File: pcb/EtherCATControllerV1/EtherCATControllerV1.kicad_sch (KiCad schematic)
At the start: 0 parts

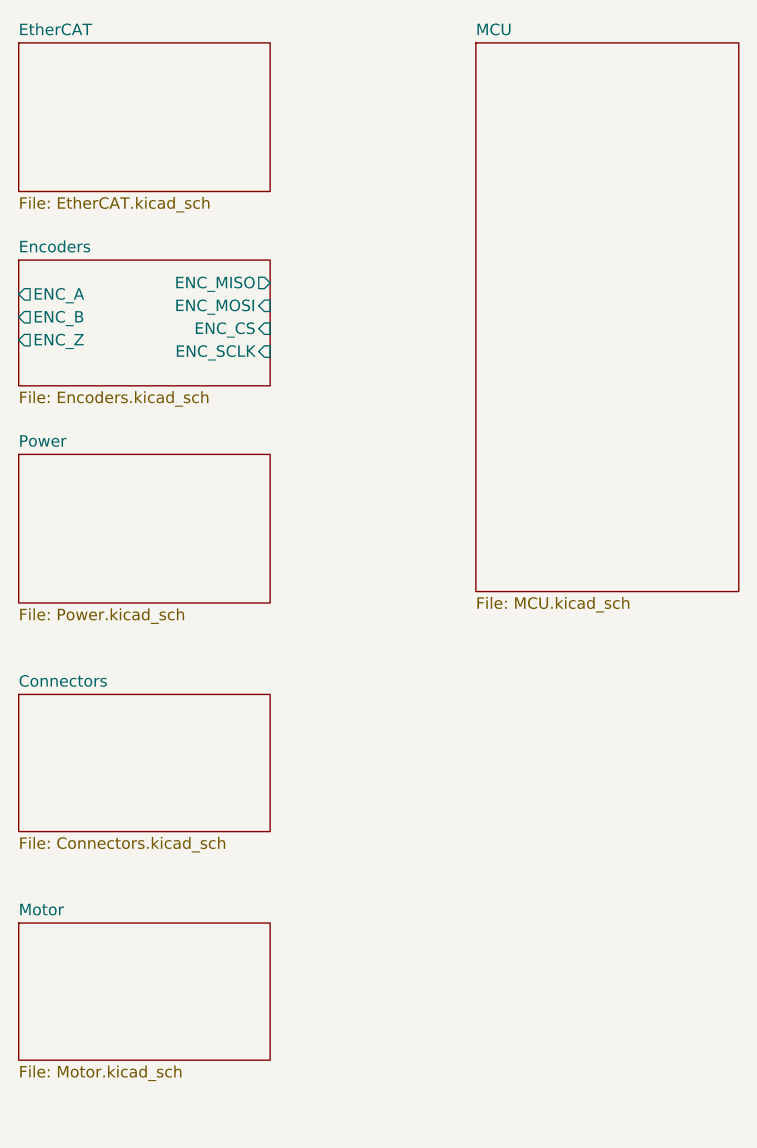
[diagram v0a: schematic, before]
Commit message: Initial design without Ethernet connectors
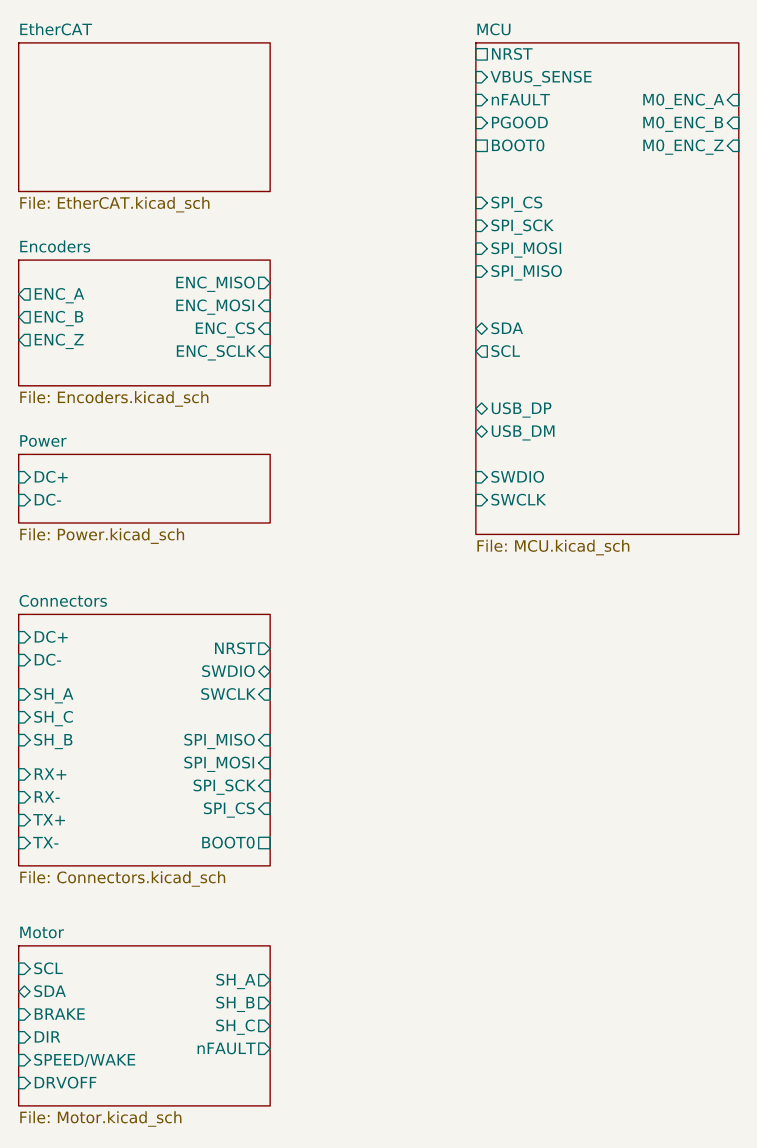
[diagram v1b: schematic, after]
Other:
- sheet Connectors ports: added BOOT0, DC+, DC-, NRST, RX+, RX-, SH_A, SH_B, SH_C, SPI_CS, SPI_MISO, SPI_MOSI, SPI_SCK, SWCLK, SWDIO, TX+, TX-; removed none
- sheet MCU ports: added BOOT0, M0_ENC_A, M0_ENC_B, M0_ENC_Z, NRST, PGOOD, SCL, SDA, SPI_CS, SPI_MISO, SPI_MOSI, SPI_SCK, SWCLK, SWDIO, USB_DM, USB_DP, VBUS_SENSE, nFAULT; removed none
- sheet Motor ports: added BRAKE, DIR, DRVOFF, SCL, SDA, SH_A, SH_B, SH_C, SPEED/WAKE, nFAULT; removed none
- sheet Power ports: added DC+, DC-; removed none

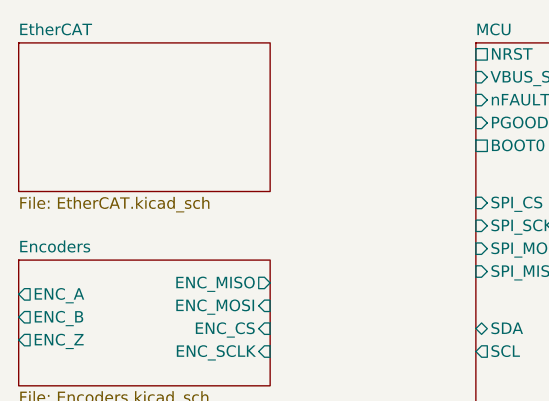
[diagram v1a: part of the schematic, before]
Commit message: Added IO Board project
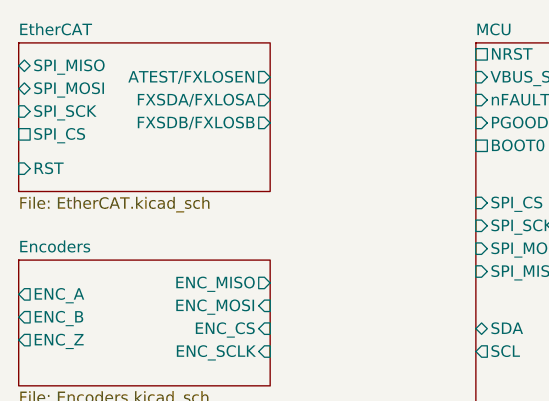
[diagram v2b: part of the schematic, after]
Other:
- sheet EtherCAT ports: added ATEST/FXLOSEN, FXSDA/FXLOSA, FXSDB/FXLOSB, RST, SPI_CS, SPI_MISO, SPI_MOSI, SPI_SCK; removed none
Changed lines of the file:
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@@
+			)
+		)
+		(pin "SPI_MISO" bidirectional
+			(at 38.1 27.94 180)
+			(effects
+				(font
+					(size 1.27 1.27)
+				)
+				(justify left)
+			)
+		)
+		(pin "SPI_MOSI" bidirectional
+			(at 38.1 30.48 180)
+			(effects
+				(font
+					(size 1.27 1.27)
+				)
+				(justify left)
+			)
+		)
+		(pin "SPI_SCK" input
+			(at 38.1 33.02 180)
+			(effects
+				(font
+					(size 1.27 1.27)
+				)
+				(justify left)
+			)
+		)
+		(pin "RST" input
+			(at 38.1 39.37 180)
+			(effects
+				(font
+					(size 1.27 1.27)
+				)
+				(justify left)
+			)
+		)
+		(pin "ATEST{slash}FXLOSEN" output
+			(at 66.04 29.21 0)
+			(effects
+				(font
+					(size 1.27 1.27)
+				)
+				(justify right)
+			)
+		)
+		(pin "FXSDB{slash}FXLOSB" output
+			(at 66.04 34.29 0)
+			(effects
+				(font
+					(size 1.27 1.27)
+				)
+				(justify right)
+			)
+		)
+		(pin "FXSDA{slash}FXLOSA" output
+			(at 66.04 31.75 0)
+			(effects
+				(font
+					(size 1.27 1.27)
+				)
+				(justify right)
+			)
+		)
+		(pin "SPI_CS" passive
+			(at 38.1 35.56 180)
+			(effects
+				(font
+					(size 1.27 1.27)
+				)
+				(justify left)
 			)
 		)

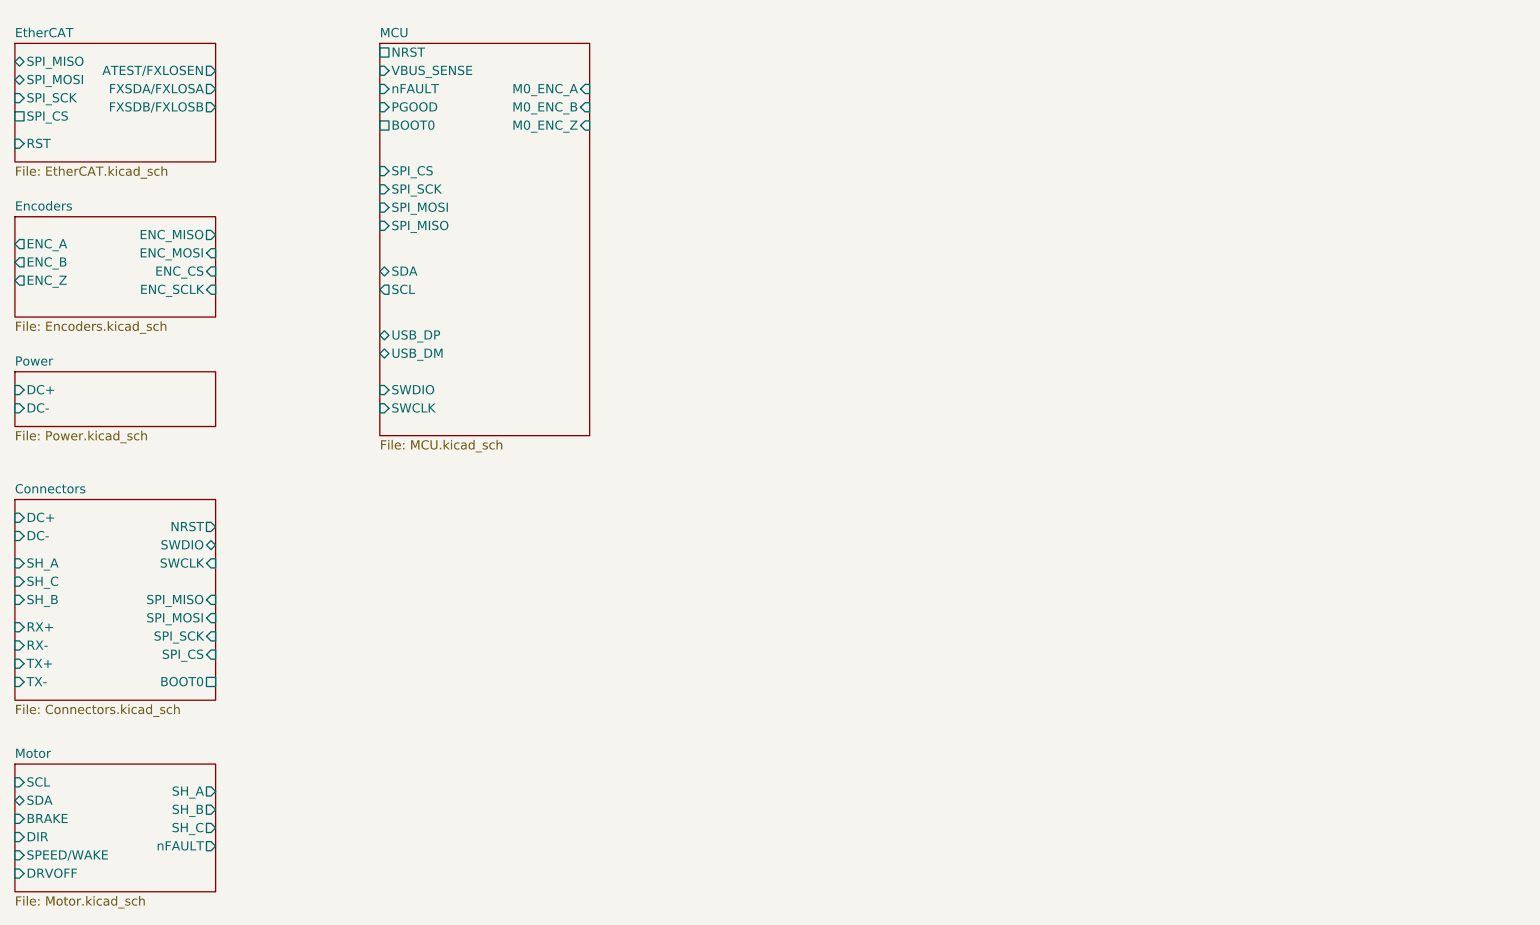
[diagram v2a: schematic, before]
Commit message: schematic finished, need to set proper ERCs
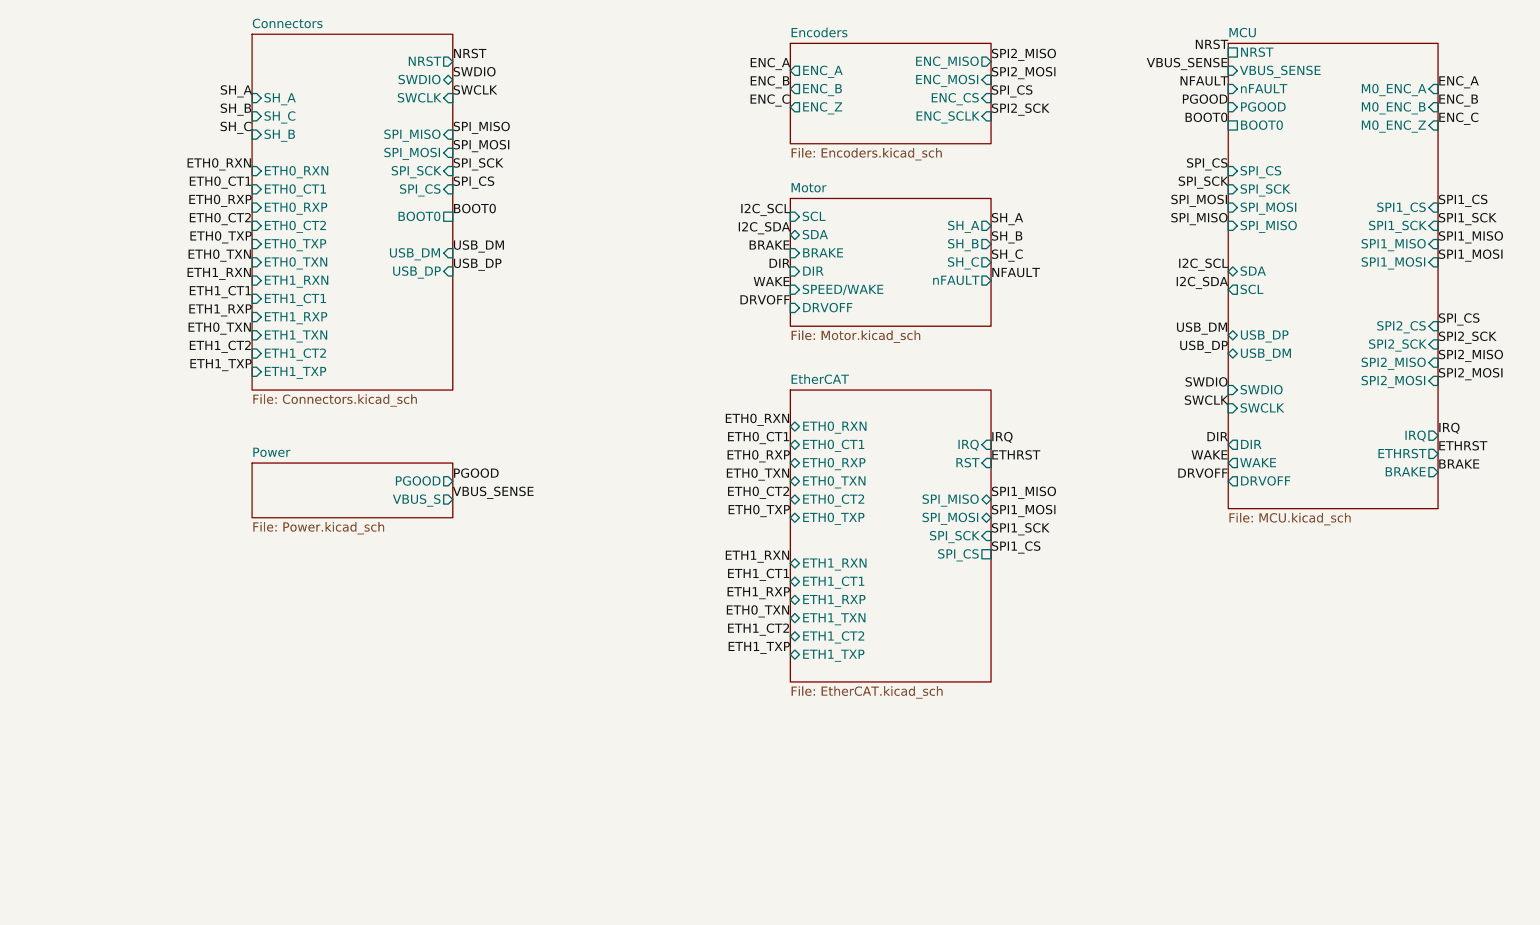
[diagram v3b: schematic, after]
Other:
- sheet Connectors ports: added ETH0_CT1, ETH0_CT2, ETH0_RXN, ETH0_RXP, ETH0_TXN, ETH0_TXP, ETH1_CT1, ETH1_CT2, ETH1_RXN, ETH1_RXP, ETH1_TXN, ETH1_TXP, USB_DM, USB_DP; removed DC+, DC-, RX+, RX-, TX+, TX-
- sheet EtherCAT ports: added ETH0_CT1, ETH0_CT2, ETH0_RXN, ETH0_RXP, ETH0_TXN, ETH0_TXP, ETH1_CT1, ETH1_CT2, ETH1_RXN, ETH1_RXP, ETH1_TXN, ETH1_TXP, IRQ; removed ATEST/FXLOSEN, FXSDA/FXLOSA, FXSDB/FXLOSB
- sheet MCU ports: added BRAKE, DIR, DRVOFF, ETHRST, IRQ, SPI1_CS, SPI1_MISO, SPI1_MOSI, SPI1_SCK, SPI2_CS, SPI2_MISO, SPI2_MOSI, SPI2_SCK, WAKE; removed none
- sheet Power ports: added PGOOD, VBUS_S; removed DC+, DC-

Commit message: Added more BOM items
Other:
- sheet MCU ports: added NFAULT; removed nFAULT
- sheet Motor ports: added NFAULT; removed nFAULT
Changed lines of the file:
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@@
-			)
-		)
-		(pin "nFAULT" output
-			(at 173.99 58.42 0)
-			(effects
-				(font
-					(size 1.27 1.27)
-				)
-				(justify right)
 			)
 		)
@@
 				)
 				(justify left)
+			)
+		)
+		(pin "NFAULT" output
+			(at 173.99 58.42 0)
+			(effects
+				(font
+					(size 1.27 1.27)
+				)
+				(justify right)
 			)
 		)
@@
 			)
 		)
-		(pin "nFAULT" input
-			(at 207.01 31.75 180)
-			(effects
-				(font
-					(size 1.27 1.27)
-				)
-				(justify left)
-			)
-		)
 		(pin "SPI_SCK" input
 			(at 207.01 45.72 180)
@@
 			)
 		)
+		(pin "NFAULT" input
+			(at 207.01 31.75 180)
+			(effects
+				(font
+					(size 1.27 1.27)
+				)
+				(justify left)
+			)
+		)
